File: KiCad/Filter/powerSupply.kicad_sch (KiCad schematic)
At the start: 0 parts

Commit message: Included MCP5211 in KiCad symbols
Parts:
- added U2: MIC5211-LXYM6-TR, SOT-23-6_M6_MCH, symbol Misc:MIC5211-LXYM6-TR
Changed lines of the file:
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@@
 	(generator_version "9.0")
 	(paper "A4")
+	(symbol
+		(lib_id "Misc:MIC5211-LXYM6-TR")
+		(at 138.43 59.69 0)
+		(unit 1)
+		(exclude_from_sim no)
+		(in_bom yes)
+		(on_board yes)
+		(dnp no)
+		(fields_autoplaced yes)
+		(property "Reference" "U2"
+			(at 138.43 45.72 0)
+			(effects
+				(font
+					(size 1.524 1.524)
+				)
+			)
+		)
+		(property "Value" "MIC5211-LXYM6-TR"
+			(at 138.43 48.26 0)
+			(effects
+				(font
+					(size 1.524 1.524)
+				)
+			)
+		)
+		(property "Footprint" "SOT-23-6_M6_MCH"
+			(at 138.938 63.246 0)
+			(effects
+				(font
+					(size 1.27 1.27)
+					(italic yes)
+				)
+				(hide yes)
+			)
+		)
+		(property "Datasheet" "MIC5211-LXYM6-TR"
+			(at 138.938 55.88 0)
+			(effects
+				(font
+					(size 1.27 1.27)
+					(italic yes)
+				)
+				(hide yes)
+			)
+		)
+		(property "Description" ""
+			(at 138.43 59.69 0)
+			(effects
+				(font
+					(size 1.27 1.27)
+				)
+				(hide yes)
+			)
+		)
+		(pin "1"
+		)
+		(pin "5"
+		)
+		(pin "6"
+		)
+		(pin "2"
+		)
+		(pin "3"
+		)
+		(pin "4"
+		)
+		(instances
+			(project ""
+				(path "/8ea2dc21-a8e6-4e4a-8986-17442369c6c0/f4d24c15-b9a1-4709-a145-87d4fc451040"
+					(reference "U2")
+					(unit 1)
+				)
+			)
+		)
+	)
 )

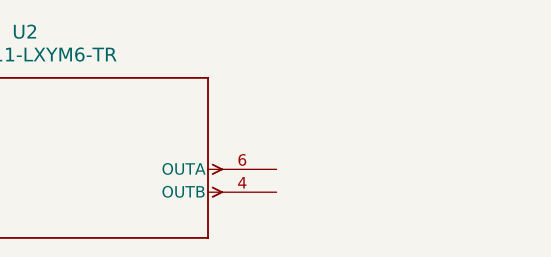
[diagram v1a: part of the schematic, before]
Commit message: VCO circuit added to schematic.
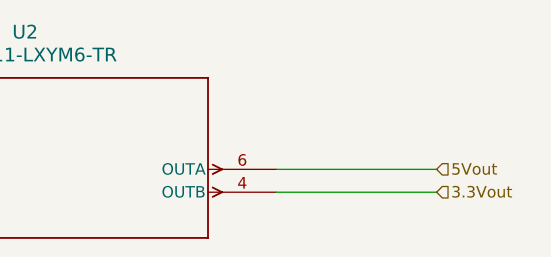
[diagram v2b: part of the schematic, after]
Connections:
- net 3.3Vout: now reaches U2.4 (OUTB)
- net 5Vout: now reaches U2.6 (OUTA)
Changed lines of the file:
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@@
 	(generator_version "9.0")
 	(paper "A4")
+	(wire
+		(pts
+			(xy 166.37 60.96) (xy 184.15 60.96)
+		)
+		(stroke
+			(width 0)
+			(type default)
+		)
+	)
+	(wire
+		(pts
+			(xy 166.37 63.5) (xy 184.15 63.5)
+		)
+		(stroke
+			(width 0)
+			(type default)
+		)
+	)
+	(hierarchical_label "3.3Vout"
+		(shape input)
+		(at 184.15 63.5 0)
+		(effects
+			(font
+				(size 1.27 1.27)
+			)
+			(justify left)
+		)
+	)
+	(hierarchical_label "5Vout"
+		(shape input)
+		(at 184.15 60.96 0)
+		(effects
+			(font
+				(size 1.27 1.27)
+			)
+			(justify left)
+		)
+	)
 	(symbol
 		(lib_id "Misc:MIC5211-LXYM6-TR")

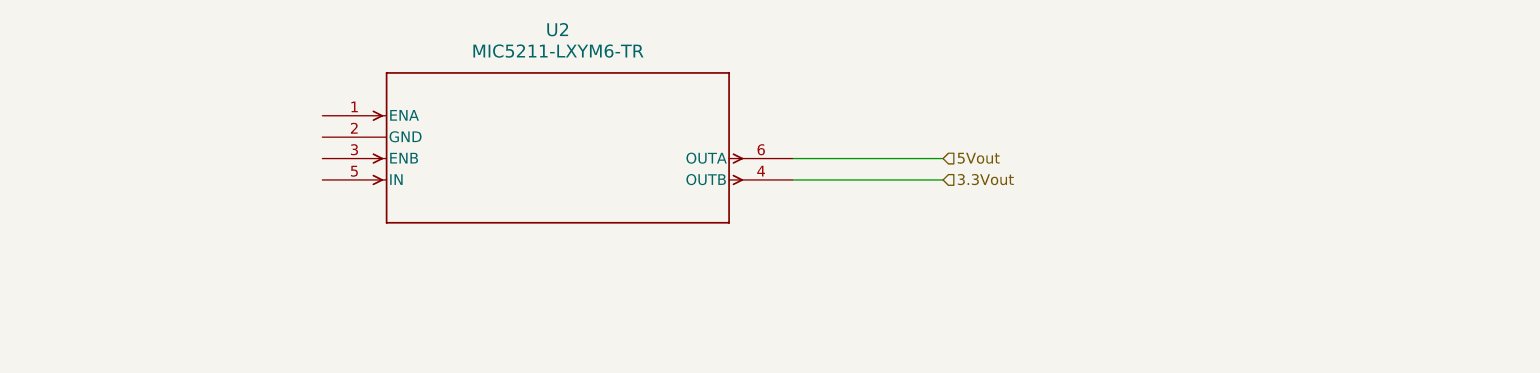
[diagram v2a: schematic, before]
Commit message: Added input jacks and bypass switch. Finished pwr supply except for 9v connection.
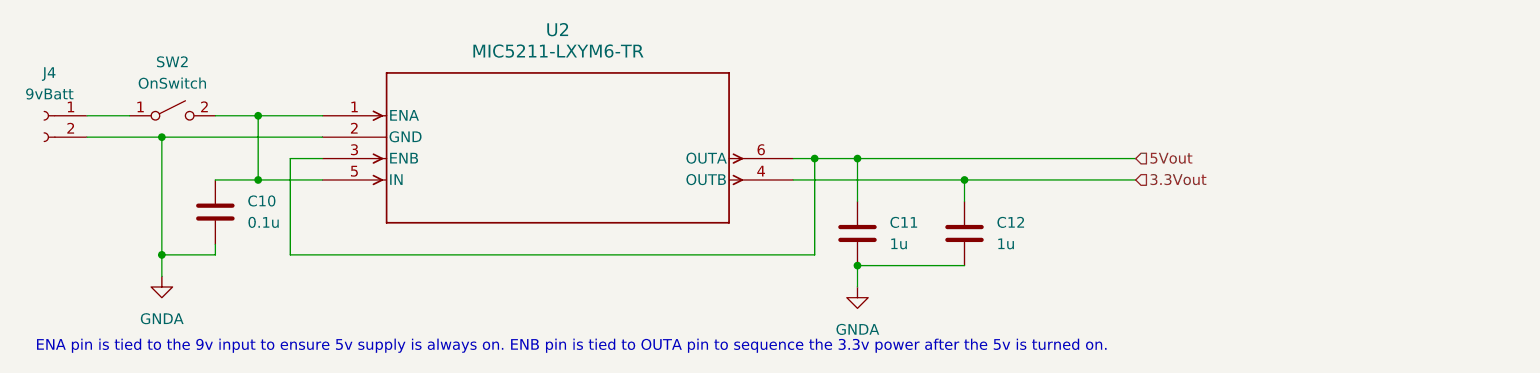
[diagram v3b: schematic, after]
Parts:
- added C10: 0.1u, symbol Device:C
- added C11, C12: 1u, symbol Device:C
- added J4: 9vBatt, symbol Connector:Conn_01x02_Socket
- added SW2: OnSwitch, symbol Switch:SW_SPST
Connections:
- net 3.3Vout: now also C12.1
- net 5Vout: now also U2.3 (ENB), C11.1
- net at U2.1 (ENA): now also U2.5 (IN), C10.2, SW2.2 (B)
- net GNDA: now reaches U2.2 (GND)
- net GNDA: now also C10.1, C11.2, C12.2, J4.2 (Pin_2)
- new net: J4.1 (Pin_1), SW2.1 (A)
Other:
- note added: "ENA pin is tied to the 9v input to ensure 5v supply is always on. ENB pin is tied to OUTA pin to sequence the 3.3v power after the 5v is turned on."
